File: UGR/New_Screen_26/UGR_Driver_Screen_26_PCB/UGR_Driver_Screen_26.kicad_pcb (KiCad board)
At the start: 2 copper layers, 133.5 x 84 mm, 64 parts, among them J2 USB_B_Micro, J3 Conn_02x20_Socket, J4 Conn_01x06, U1 TPS562200, U2 STM32F767VGTx, U3 SI2347DS-T1-GE3, U4 MCP2562-E-MF, U5 SI2347DS-T1-GE3, U6 SI2347DS-T1-GE3, U7 SI2347DS-T1-GE3, U8 SI2347DS-T1-GE3, U9 SI2347DS-T1-GE3

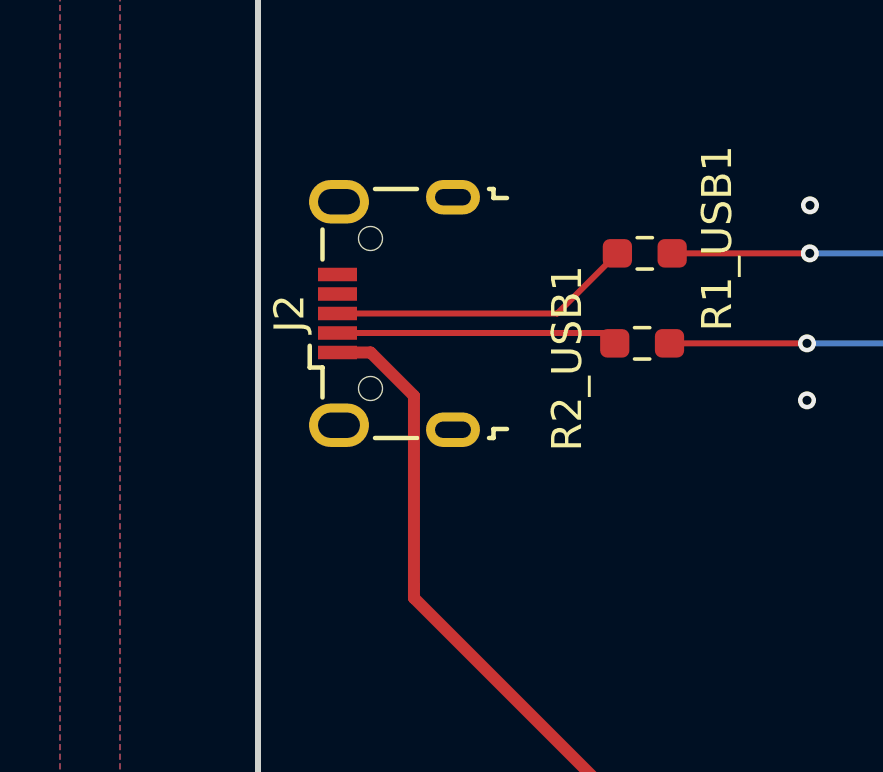
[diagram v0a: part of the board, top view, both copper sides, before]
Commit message: Full UGR Screen 26 Code + Rover
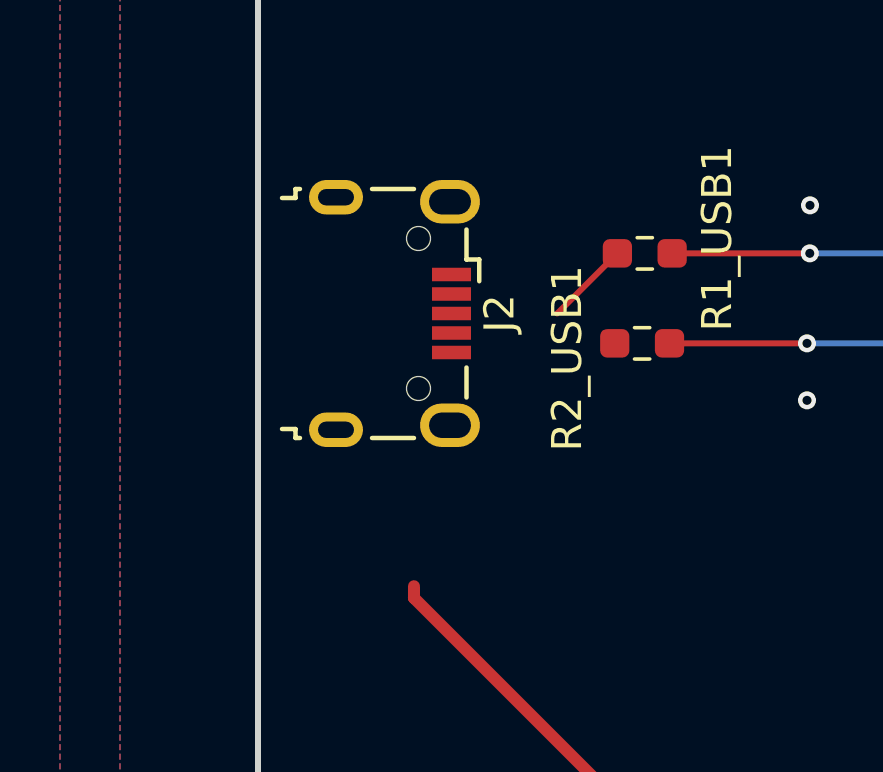
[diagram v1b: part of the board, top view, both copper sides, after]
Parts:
- turned J2 to -90 degrees
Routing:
- net 5V USB: track 26.6 -> 17.1 mm
- net Net-(J2-D-): track 9.39 -> 0.49 mm
- net Net-(J2-D+): track 10.2 -> 2.84 mm
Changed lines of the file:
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@@
 	(footprint "Connector_USB:USB_Micro-B_Wuerth_629105150521"
 		(layer "F.Cu")
-		(at 84.55 89.005 90)
+		(at 84.55 89.005 -90)
 		(descr "USB Micro-B receptacle, http://www.mouser.com/ds/2/445/629105150521-469306.pdf")
 		(tags "usb micro receptacle")
@@
 		)
 		(property "Datasheet" "~"
-			(at 0 0 90)
+			(at 0 0 270)
 			(unlocked yes)
 			(layer "F.Fab")
@@
 		)
 		(property "Description" "USB Micro Type B connector"
-			(at 0 0 90)
+			(at 0 0 270)
 			(unlocked yes)
 			(layer "F.Fab")
@@
 		(attr smd)
 		(fp_line
-			(start -1.075 -2.825)
-			(end -1.8 -2.825)
+			(start 3.85 3.75)
+			(end 3.85 3.3)
 			(stroke
 				(width 0.15)
@@
 		)
 		(fp_line
-			(start -1.8 -2.825)
-			(end -1.8 -2.4)
+			(start -4.15 3.3)
+			(end -3.85 3.3)
 			(stroke
 				(width 0.15)
@@
 		)
 		(fp_line
-			(start 1.8 -2.4)
-			(end 2.8 -2.4)
+			(start -3.85 3.3)
+			(end -3.85 3.75)
 			(stroke
 				(width 0.15)
@@
 		)
 		(fp_line
-			(start -1.8 -2.4)
-			(end -2.8 -2.4)
+			(start 3.85 3.3)
+			(end 4.15 3.3)
 			(stroke
 				(width 0.15)
@@
 		)
 		(fp_line
-			(start -4.15 -0.65)
-			(end -4.15 0.75)
+			(start 4.15 3.3)
+			(end 4.15 3.15)
 			(stroke
 				(width 0.15)
@@
 		)
 		(fp_line
-			(start 4.15 0.75)
-			(end 4.15 -0.65)
+			(start -4.15 3.15)
+			(end -4.15 3.3)
 			(stroke
 				(width 0.15)
@@
 		)
 		(fp_line
-			(start -4.15 3.15)
-			(end -4.15 3.3)
+			(start 4.15 0.75)
+			(end 4.15 -0.65)
 			(stroke
 				(width 0.15)
@@
 		)
 		(fp_line
-			(start 4.15 3.3)
-			(end 4.15 3.15)
+			(start -4.15 -0.65)
+			(end -4.15 0.75)
 			(stroke
 				(width 0.15)
@@
 		)
 		(fp_line
-			(start 3.85 3.3)
-			(end 4.15 3.3)
+			(start -1.8 -2.4)
+			(end -2.8 -2.4)
 			(stroke
 				(width 0.15)
@@
 		)
 		(fp_line
-			(start -3.85 3.3)
-			(end -3.85 3.75)
+			(start 1.8 -2.4)
+			(end 2.8 -2.4)
 			(stroke
 				(width 0.15)
@@
 		)
 		(fp_line
-			(start -4.15 3.3)
-			(end -3.85 3.3)
+			(start -1.8 -2.825)
+			(end -1.8 -2.4)
 			(stroke
 				(width 0.15)
@@
 		)
 		(fp_line
-			(start 3.85 3.75)
-			(end 3.85 3.3)
+			(start -1.075 -2.825)
+			(end -1.8 -2.825)
 			(stroke
 				(width 0.15)
@@
 		)
 		(fp_line
-			(start 4.95 -3.34)
-			(end -4.94 -3.34)
+			(start -4.94 4.85)
+			(end 4.95 4.85)
 			(stroke
 				(width 0.05)
@@
 		)
 		(fp_line
-			(start -4.94 -3.34)
-			(end -4.94 4.85)
+			(start 4.95 4.85)
+			(end 4.95 -3.34)
 			(stroke
 				(width 0.05)
@@
 		)
 		(fp_line
-			(start 4.95 4.85)
-			(end 4.95 -3.34)
+			(start -4.94 -3.34)
+			(end -4.94 4.85)
 			(stroke
 				(width 0.05)
@@
 		)
 		(fp_line
-			(start -4.94 4.85)
-			(end 4.95 4.85)
+			(start 4.95 -3.34)
+			(end -4.94 -3.34)
 			(stroke
 				(width 0.05)
@@
 		)
 		(fp_line
-			(start -1.075 -2.95)
-			(end -1.075 -2.725)
+			(start -3.7 4.35)
+			(end 3.7 4.35)
 			(stroke
 				(width 0.15)
@@
 		)
 		(fp_line
-			(start -1.525 -2.95)
-			(end -1.075 -2.95)
+			(start 3.7 4.35)
+			(end 3.7 3.15)
 			(stroke
 				(width 0.15)
@@
 		)
 		(fp_line
-			(start -1.075 -2.725)
-			(end -1.3 -2.55)
+			(start -2.7 3.75)
+			(end 2.7 3.75)
 			(stroke
 				(width 0.15)
@@
 		)
 		(fp_line
-			(start -1.525 -2.725)
-			(end -1.525 -2.95)
+			(start -4 3.15)
+			(end -3.7 3.15)
 			(stroke
 				(width 0.15)
@@
 		)
 		(fp_line
-			(start -1.3 -2.55)
-			(end -1.525 -2.725)
+			(start -3.7 3.15)
+			(end -3.7 4.35)
 			(stroke
 				(width 0.15)
@@
 		)
 		(fp_line
-			(start 4 -2.25)
-			(end -4 -2.25)
+			(start 3.7 3.15)
+			(end 4 3.15)
 			(stroke
 				(width 0.15)
@@
 		)
 		(fp_line
-			(start -4 -2.25)
-			(end -4 3.15)
+			(start 4 3.15)
+			(end 4 -2.25)
 			(stroke
 				(width 0.15)
@@
 		)
 		(fp_line
-			(start 4 3.15)
-			(end 4 -2.25)
+			(start -4 -2.25)
+			(end -4 3.15)
 			(stroke
 				(width 0.15)
@@
 		)
 		(fp_line
-			(start 3.7 3.15)
-			(end 4 3.15)
+			(start 4 -2.25)
+			(end -4 -2.25)
 			(stroke
 				(width 0.15)
@@
 		)
 		(fp_line
-			(start -3.7 3.15)
-			(end -3.7 4.35)
+			(start -1.3 -2.55)
+			(end -1.525 -2.725)
 			(stroke
 				(width 0.15)
@@
 		)
 		(fp_line
-			(start -4 3.15)
-			(end -3.7 3.15)
+			(start -1.525 -2.725)
+			(end -1.525 -2.95)
 			(stroke
 				(width 0.15)
@@
 		)
 		(fp_line
-			(start -2.7 3.75)
-			(end 2.7 3.75)
+			(start -1.075 -2.725)
+			(end -1.3 -2.55)
 			(stroke
 				(width 0.15)
@@
 		)
 		(fp_line
-			(start 3.7 4.35)
-			(end 3.7 3.15)
+			(start -1.525 -2.95)
+			(end -1.075 -2.95)
 			(stroke
 				(width 0.15)
@@
 		)
 		(fp_line
-			(start -3.7 4.35)
-			(end 3.7 4.35)
+			(start -1.075 -2.95)
+			(end -1.075 -2.725)
 			(stroke
 				(width 0.15)
@@
 		)
 		(pad "" np_thru_hole oval
-			(at -2.5 -0.8 90)
+			(at -2.5 -0.8 270)
 			(size 0.8 0.8)
 			(drill 0.8)
@@
 		)
 		(pad "" np_thru_hole oval
-			(at 2.5 -0.8 90)
+			(at 2.5 -0.8 270)
 			(size 0.8 0.8)
 			(drill 0.8)
@@
 		)
 		(pad "1" smd rect
-			(at -1.3 -1.9 90)
+			(at -1.3 -1.9 270)
 			(size 0.45 1.3)
 			(layers "F.Cu" "F.Mask" "F.Paste")
@@
 		)
 		(pad "2" smd rect
-			(at -0.65 -1.9 90)
+			(at -0.65 -1.9 270)
 			(size 0.45 1.3)
 			(layers "F.Cu" "F.Mask" "F.Paste")
@@
 		)
 		(pad "3" smd rect
-			(at 0 -1.9 90)
+			(at 0 -1.9 270)
 			(size 0.45 1.3)
 			(layers "F.Cu" "F.Mask" "F.Paste")
@@
 		)
 		(pad "4" smd rect
-			(at 0.65 -1.9 90)
+			(at 0.65 -1.9 270)
 			(size 0.45 1.3)
 			(layers "F.Cu" "F.Mask" "F.Paste")
@@
 		)
 		(pad "5" smd rect
-			(at 1.3 -1.9 90)
+			(at 1.3 -1.9 270)
 			(size 0.45 1.3)
 			(layers "F.Cu" "F.Mask" "F.Paste")
@@
 		)
 		(pad "6" thru_hole oval
-			(at -3.875 1.95 90)
+			(at -3.875 1.95 270)
 			(size 1.15 1.8)
 			(drill oval 0.55 1.2)
@@
 		)
 		(pad "6" thru_hole oval
-			(at -3.725 -1.85 90)
+			(at -3.725 -1.85 270)
 			(size 1.45 2)
 			(drill oval 0.85 1.4)
@@
 		)
 		(pad "6" thru_hole oval
-			(at 3.725 -1.85 90)
+			(at 3.725 -1.85 270)
 			(size 1.45 2)
 			(drill oval 0.85 1.4)
@@
 		)
 		(pad "6" thru_hole oval
-			(at 3.875 1.95 90)
+			(at 3.875 1.95 270)
 			(size 1.15 1.8)
 			(drill oval 0.55 1.2)
@@
 	)
 	(segment
-		(start 83.753496 90.305)
-		(end 85.199 91.750504)
-		(width 0.4)
-		(layer "F.Cu")
-		(net 14)
-	)
-	(segment
-		(start 82.65 90.305)
-		(end 83.753496 90.305)
-		(width 0.4)
-		(layer "F.Cu")
-		(net 14)
-	)
-	(segment
 		(start 85.199 98.0951)
 		(end 85.199 98.4876)
@@
 	)
 	(segment
-		(start 85.199 91.750504)
-		(end 85.199 98.0951)
-		(width 0.4)
-		(layer "F.Cu")
-		(net 14)
-	)
-	(segment
 		(start 128.55 95.025)
 		(end 130.89992 95.025)
@@
 	)
 	(segment
-		(start 91.5475 89.655)
-		(end 82.65 89.655)
-		(width 0.2)
-		(layer "F.Cu")
-		(net 20)
-	)
-	(segment
 		(start 91.8925 90)
 		(end 91.5475 89.655)
@@
 		(width 0.2)
 		(layer "F.Cu")
-		(net 21)
-	)
-	(segment
-		(start 82.65 89.005)
-		(end 89.975 89.005)
-		(width 0.2)
-		(layer "F.Cu")

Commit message: Rover + UGR Screen PCB
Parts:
- removed D4: BZX384xxxx, Diode_SMD:D_SOD-323
- removed F1: 0.75A, Fuse:Fuse_1812_4532Metric_Pad1.30x3.40mm_HandSolder
- removed J4: Conn_01x06, Connector_PinHeader_2.54mm:PinHeader_1x06_P2.54mm_Vertical
- removed Main_Conn1: Conn_01x04, UGR:Bulgin_4_Pin
- removed Main_Conn_Parallel1: Conn_01x04, Connector_PinHeader_2.54mm:PinHeader_1x04_P2.54mm_Vertical
- removed R1_POWER1, R1_POWER2, R1_POWER3, R1_POWER4, R1_POWER5, R1_POWER6: 47k, Resistor_SMD:R_0603_1608Metric_Pad0.98x0.95mm_HandSolder
- removed R1_USB1, R2_USB1: 22R, Resistor_SMD:R_0603_1608Metric_Pad0.98x0.95mm_HandSolder
- removed U4: MCP2562-E-MF, Package_SO:SOIC-8_3.9x4.9mm_P1.27mm
- removed U6, U7, U8, U9: SI2347DS-T1-GE3, SI2347DS-T1-GE3:SOT_7DS-T1-GE3_VIS
- added CONN1: PXP4013/08P/PC, Apps:Bulgin_4000_PXP4013-08S-PC, F.Cu at (136.2, 77.9)
- added C_SD1: 0.1u, Capacitor_SMD:C_0603_1608Metric_Pad1.08x0.95mm_HandSolder, F.Cu at (106.7, 83.6)
- added C_TPS1: 0.1u, Capacitor_SMD:C_0603_1608Metric_Pad1.08x0.95mm_HandSolder, F.Cu at (93.9, 119.5)
- added C_TPS2: 0.1u, Capacitor_SMD:C_0603_1608Metric_Pad1.08x0.95mm_HandSolder, F.Cu at (96.9, 120.0)
- added C_TPS3: 0.1u, Capacitor_SMD:C_0603_1608Metric_Pad1.08x0.95mm_HandSolder, F.Cu at (96.9, 123.8)
- added D5: BZX384x, Diode_SMD:D_SOD-323, F.Cu at (176.3, 73.7)
- added D7: BZX384xxxx, Diode_SMD:D_SOD-323, F.Cu at (137.0, 91.1)
- added F2: 0.75A, Fuse:Fuse_1812_4532Metric_Pad1.30x3.40mm_HandSolder, F.Cu at (173.0, 70.1)
- added F3: 0.75A, Fuse:Fuse_1812_4532Metric_Pad1.30x3.40mm_HandSolder, F.Cu at (132.4, 91.1)
- added G***: LOGO, UGR:UGR_ALL_SILK_40mm, F.Cu at (105.9, 70.9)
- added J1: 2171790001, UGR:MOLEX_2171790001, F.Cu at (167.7, 63.6)
- added J5: Conn_01x06, Connector_PinHeader_2.54mm:PinHeader_1x06_P2.54mm_Vertical, F.Cu at (143.3, 62.0)
- added R1_CC1: 5.1k, Resistor_SMD:R_0603_1608Metric_Pad0.98x0.95mm_HandSolder, F.Cu at (168.8, 70.1)
- added R1_VBUS1: 20k, Resistor_SMD:R_0603_1608Metric_Pad0.98x0.95mm_HandSolder, F.Cu at (162.5, 93.7)
- added R2_CC1: 5.1k, Resistor_SMD:R_0603_1608Metric_Pad0.98x0.95mm_HandSolder, F.Cu at (165.8, 70.0)
- added R2_VBUS1: 10k, Resistor_SMD:R_0603_1608Metric_Pad0.98x0.95mm_HandSolder, F.Cu at (159.8, 93.7)
- added R_DISCH1: 100k, Resistor_SMD:R_0603_1608Metric_Pad0.98x0.95mm_HandSolder, F.Cu at (178.3, 70.1)
- added R_LIM1: 250, Resistor_SMD:R_0603_1608Metric_Pad0.98x0.95mm_HandSolder, F.Cu at (85.9, 123.1)
- added R_SD1: 10k, Resistor_SMD:R_0603_1608Metric_Pad0.98x0.95mm_HandSolder, F.Cu at (95.6, 90.0)
- added R_SD2: 10k, Resistor_SMD:R_0603_1608Metric_Pad0.98x0.95mm_HandSolder, F.Cu at (104.7, 91.2)
- added R_SD3: 30k, Resistor_SMD:R_0603_1608Metric_Pad0.98x0.95mm_HandSolder, F.Cu at (98.2, 87.9)
- added R_SD4: 30k, Resistor_SMD:R_0603_1608Metric_Pad0.98x0.95mm_HandSolder, F.Cu at (104.7, 94.0)
- added R_SD5: 10k, Resistor_SMD:R_0603_1608Metric_Pad0.98x0.95mm_HandSolder, F.Cu at (108.2, 89.0)
- added R_SD6: 10k, Resistor_SMD:R_0603_1608Metric_Pad0.98x0.95mm_HandSolder, F.Cu at (98.1, 84.4)
- added TPS2112APW1: ~, UGR:SOP65P640X120-8N, F.Cu at (92.0, 122.1)
- J2: value USB_B_Micro -> Conn_01x05; footprint Connector_USB:USB_Micro-B_Wuerth_629105150521 -> Connector_PinHeader_2.54mm:PinHeader_1x05_P2.54mm_Vertical
- U3: value SI2347DS-T1-GE3 -> LM358DT; footprint SI2347DS-T1-GE3:SOT_7DS-T1-GE3_VIS -> LM358:SOIC127P600X175-8N
- U5: value SI2347DS-T1-GE3 -> MCP2562-E-SN; footprint SI2347DS-T1-GE3:SOT_7DS-T1-GE3_VIS -> Package_SO:SOIC-8_3.9x4.9mm_P1.27mm
- moved U5 69.4 mm to (153.7, 78.8), turned to 180 degrees
- moved G*** 62.0 mm to (181.9, 129.2)
- moved J2 59.6 mm to (115.3, 140.0), turned to 90 degrees
- moved U3 24.3 mm to (103.1, 87.4), turned to 0 degrees
- moved C1_OSC1 4.99 mm to (171.2, 126.3), turned to 180 degrees
- moved C2_CAP1 2.84 mm to (166.2, 101.0), turned to 90 degrees
- moved D1 1.25 mm to (144.6, 81.0)
- moved S1 1.25 mm to (145.5, 140.8)
- moved C3_VDD1 1.17 mm to (164.2, 100.8), turned to 90 degrees
- renumbered D2_3V3 to D2, D3_5V to D3, REF** to MH_3.2mm
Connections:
- C16_U1 pad 1: 3V3 REG -> +3V3
- C18_U1 pad 1: 3V3 REG -> +3V3
- D1 pad 1: CANL -> CAN_N
- D1 pad 2: CANH -> CAN_P
- J2 pad 1: 5V USB -> +5V
- J2 pad 2: Net-(J2-D-) -> SWCLK
- J2 pad 3: Net-(J2-D+) -> SWDIO
- J2 pad 4: unconnected-(J2-ID-Pad4) -> NRST
- J3 pad 39: unconnected-(J3-Pin_39-Pad39) -> T_INT
- L2_U1 pad 2: 3V3 REG -> +3V3
- R10_U1 pad 1: 3V3 REG -> +3V3
- U2 pad 68: unconnected-(U2-PA9-Pad68) -> Net-(U2-PA9)
- U2 pad 70: Net-(U2-PA11) -> USB_DN
- U2 pad 71: Net-(U2-PA12) -> USB_DP
- U3 pad 1: Net-(R1_POWER5-Pad1) -> MCU_SDC+
- U3 pad 2: +5V -> MCU_SDC+
- U3 pad 3: 5V USB -> Net-(U3-IN1+)
- U5 pad 1: Net-(R1_POWER1-Pad1) -> CAN1_TX
- U5 pad 2: +5V -> GND
- U5 pad 3: 5V MAIN CON -> +5V
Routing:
- net 5V USB: track 17.1 -> 116.2 mm, vias 0 -> 4
- net Net-(U2-PA11): track 83.2 -> 0.00 mm, vias 2 -> 0
- net Net-(U2-PA12): track 83.2 -> 0.00 mm, vias 2 -> 0
- net SDC+: track 0.00 -> 81.8 mm, vias 0 -> 1
- net T_INT: track 0.00 -> 60.9 mm, vias 0 -> 1
- net SDC-: track 0.00 -> 56.1 mm, vias 0 -> 1
- net CANL: track 50.0 -> 0.00 mm
- net 5V DEBUG CON: track 48.5 -> 0.00 mm
- net +5V: track 137.5 -> 184.4 mm
- net 5V MAIN CON: track 43.4 -> 89.5 mm
- net USB_DP: track 0.00 -> 43.7 mm, vias 0 -> 2
- net USB_DN: track 0.00 -> 43.4 mm, vias 0 -> 2
- net CAN_P: track 0.00 -> 43.3 mm, vias 0 -> 1
- net CAN_N: track 0.00 -> 43.3 mm, vias 0 -> 1
- net CANH: track 31.8 -> 0.00 mm
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- removed copper zone on B.Cu, net +3V3
- removed copper zone on F.Cu, net +3V3
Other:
- board text added: "CAN_H"
- board text added: "CAN_L"
- board text added: "PCB for dashboard screen"
- board text added: "SDC+"
- board text added: "SDC-"
- board text added: "V2"
- board text removed: "3V3"
- board text removed: "H"
- board text removed: "L"
- board text removed: "PCB for 800x400 IPS screen"
- board text removed: "V1"
